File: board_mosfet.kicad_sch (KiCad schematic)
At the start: 7 parts

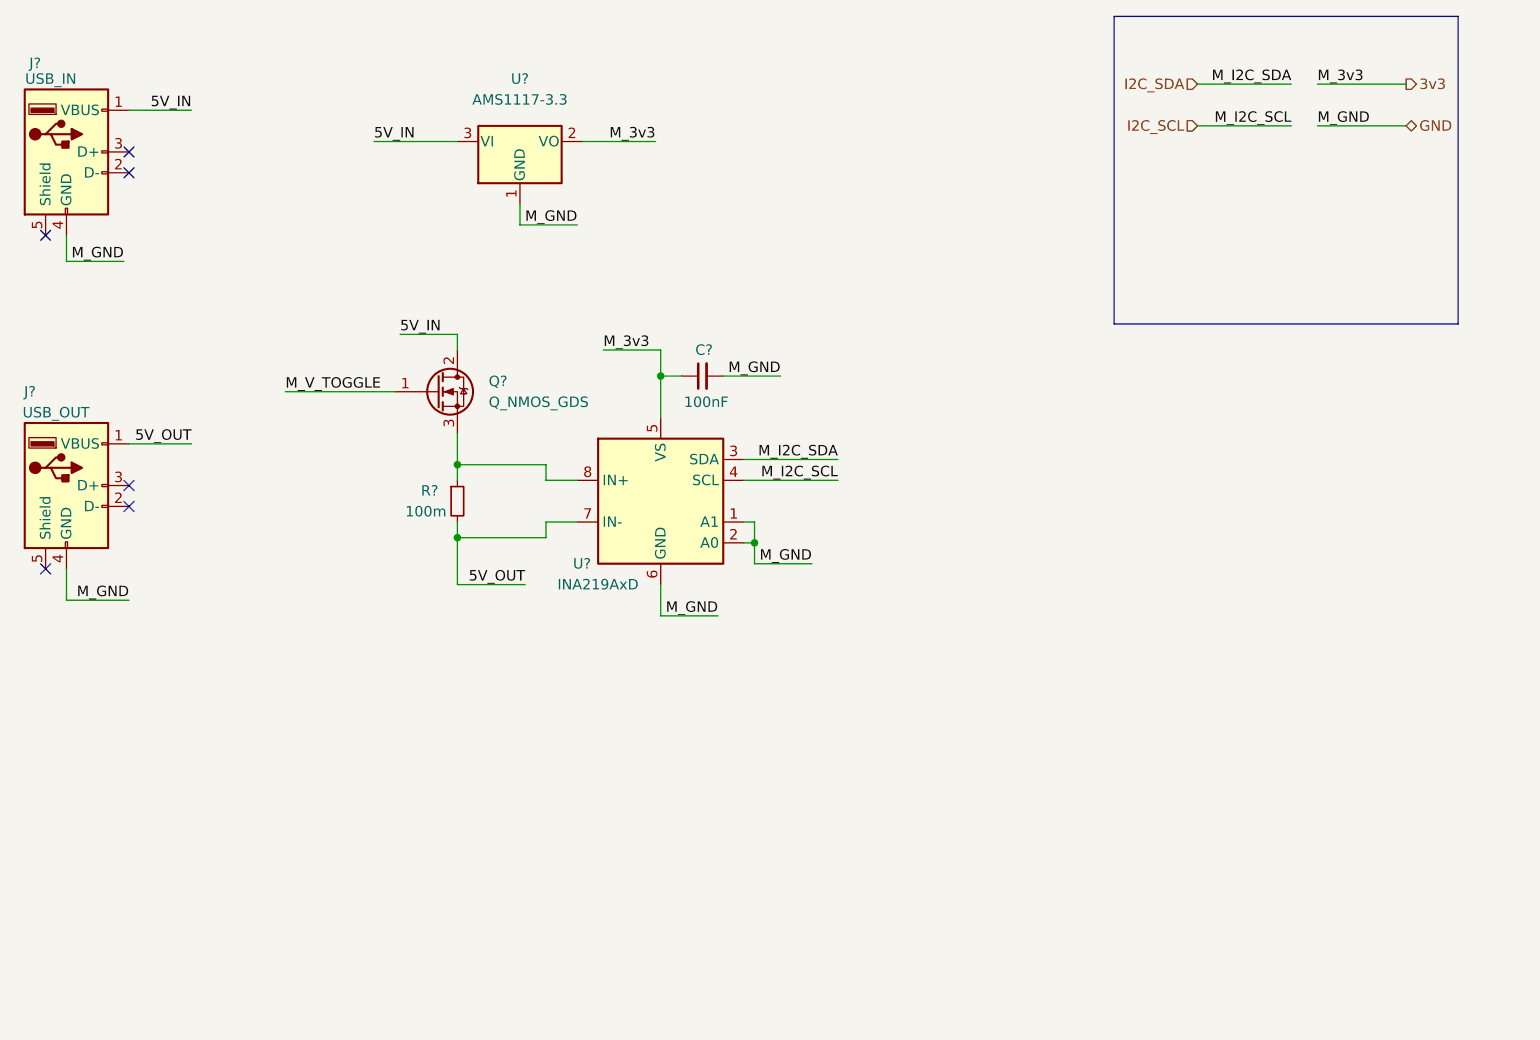
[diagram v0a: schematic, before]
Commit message: Fixed file name, started board layout
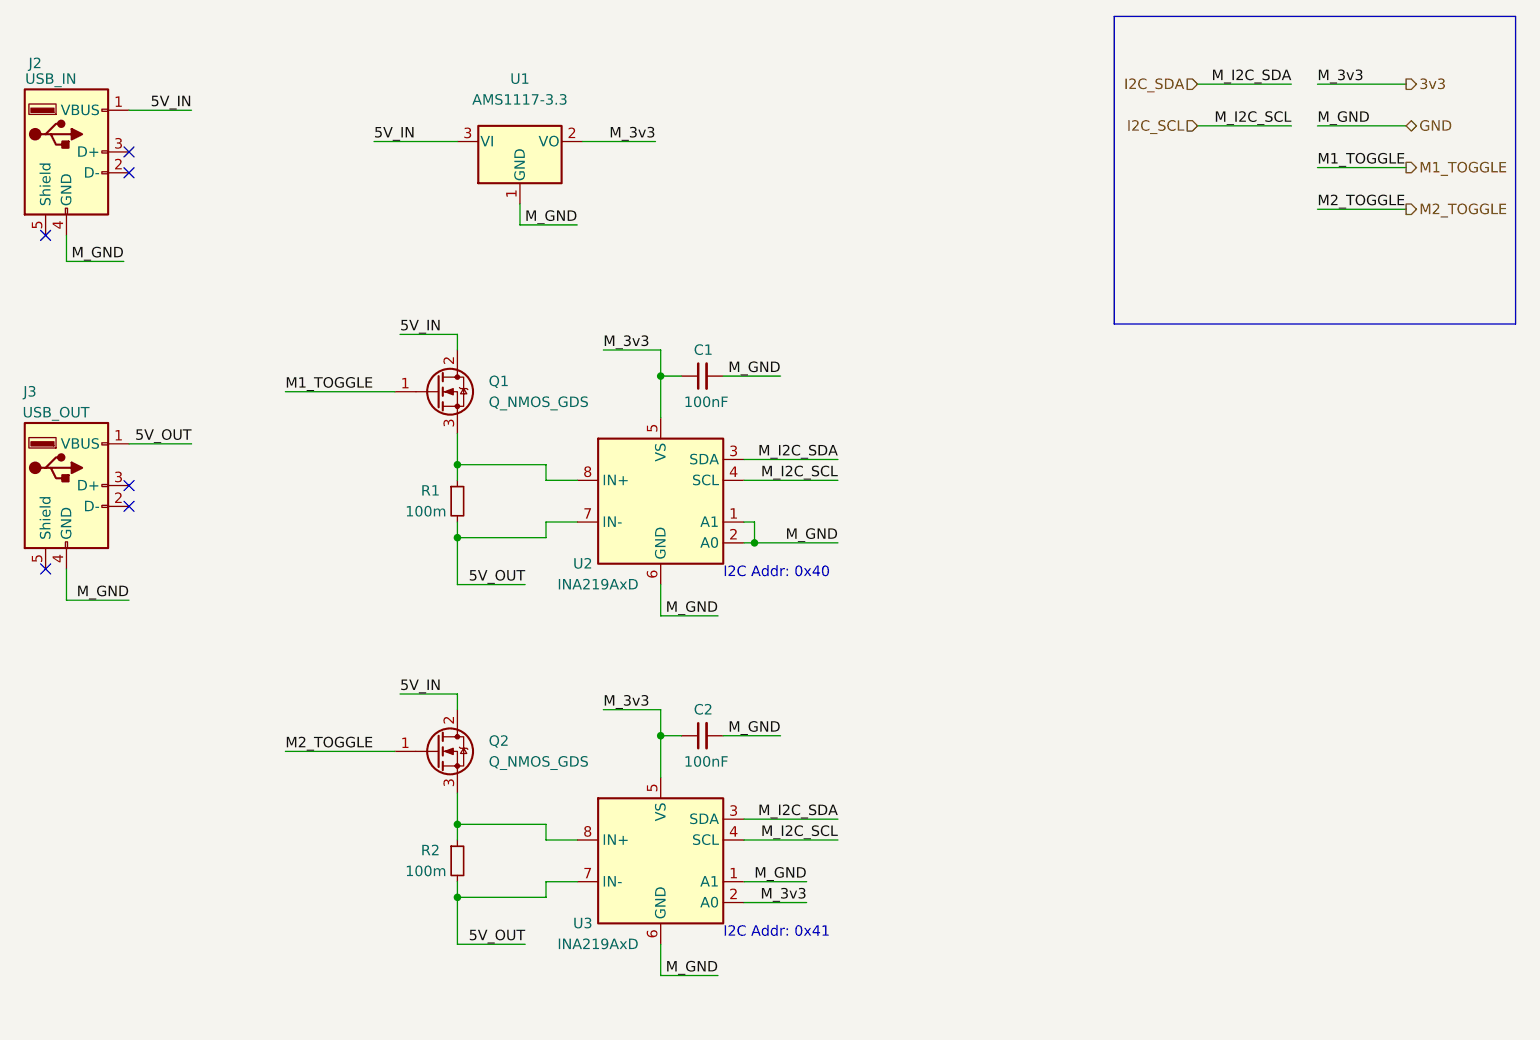
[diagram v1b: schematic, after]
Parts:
- added C2: 100nF, Capacitor_SMD:C_0402_1005Metric, symbol Device:C_Small
- added Q2: Q_NMOS_GDS, symbol Device:Q_NMOS_GDS
- added R2: 100m, Resistor_SMD:R_0402_1005Metric, symbol Device:R_Small
- added U3: INA219AxD, Package_SO:SOIC-8_3.9x4.9mm_P1.27mm, symbol Analog_ADC:INA219AxD
- C1: renamed from C?; footprint (none) -> Capacitor_SMD:C_0402_1005Metric
- R1: renamed from R?; footprint (none) -> Resistor_SMD:R_0402_1005Metric
- gave numbers to parts that had none: 5
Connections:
- net 3v3: now also C2.1, U3.2 (A0), U3.5 (VS)
- net 5V_IN: now also Q2.2 (D)
- net 5V_OUT: now also R2.2, U3.7 (IN-)
- net GND: now also C2.2, U3.1 (A1), U3.6 (GND)
- net I2C_SCL: now also U3.4 (SCL)
- net I2C_SDA: now also U3.3 (SDA)
- net M_V_TOGGLE renamed M1_TOGGLE
- new net: Q2.3 (S), R2.1, U3.8 (IN+)
- new net M2_TOGGLE: Q2.1 (G)
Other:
- note added: "I2C Addr: 0x40"
- note added: "I2C Addr: 0x41"

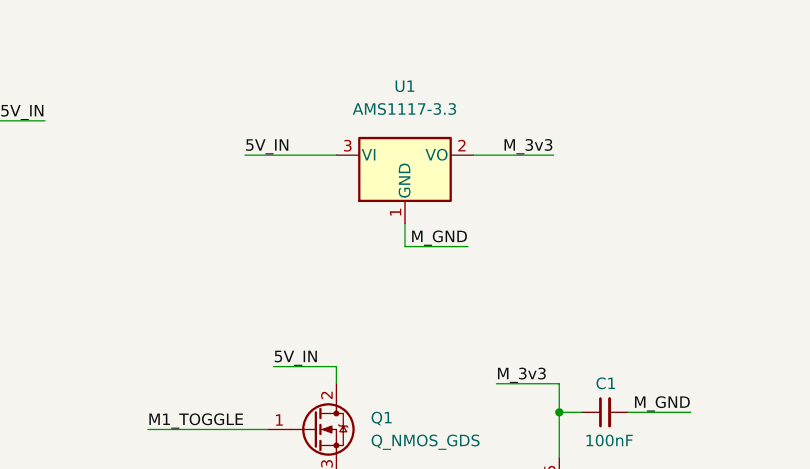
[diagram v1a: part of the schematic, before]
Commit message: Added capacitor filtering to AMS1117
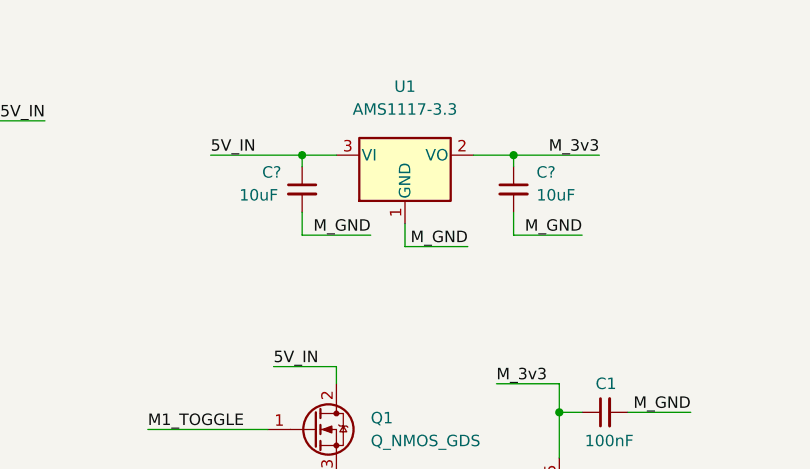
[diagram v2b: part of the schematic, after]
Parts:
- added C? (x2): 10uF, symbol Device:C_Small
- U1: LCSC Part Number (none) -> C173386; Manufacturer (none) -> Shenzhen Fuman Elec; Manufacturer Part Number (none) -> AMS1117-3.3V
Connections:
- net 3v3: now also C?.1
- net 5V_IN: now also C?.1
- net GND: now also C?.2, C?.2
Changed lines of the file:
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@@
   (junction (at 85.09 92.075) (diameter 0) (color 0 0 0 0)
   )
+  (junction (at 81.28 43.815) (diameter 0) (color 0 0 0 0)
+  )
   (junction (at 85.09 135.89) (diameter 0) (color 0 0 0 0)
+  )
+  (junction (at 104.775 43.815) (diameter 0) (color 0 0 0 0)
   )
   (no_connect (at 45.085 45.085))
@@
     (stroke (width 0) (type default) (color 0 0 0 0))
   )
+  (wire (pts (xy 104.775 43.815) (xy 114.3 43.815))
+    (stroke (width 0) (type default) (color 0 0 0 0))
+  )
   (wire (pts (xy 175.26 36.83) (xy 186.69 36.83))
     (stroke (width 0) (type default) (color 0 0 0 0))
@@
     (stroke (width 0) (type default) (color 0 0 0 0))
   )
+  (wire (pts (xy 104.775 52.705) (xy 104.775 50.165))
+    (stroke (width 0) (type default) (color 0 0 0 0))
+  )
   (wire (pts (xy 120.015 85.09) (xy 131.445 85.09))
     (stroke (width 0) (type default) (color 0 0 0 0))
@@
     (stroke (width 0) (type default) (color 0 0 0 0))
   )
-  (wire (pts (xy 74.93 43.815) (xy 85.09 43.815))
+  (wire (pts (xy 71.12 43.815) (xy 81.28 43.815))
     (stroke (width 0) (type default) (color 0 0 0 0))
   )
@@
     (stroke (width 0) (type default) (color 0 0 0 0))
   )
+  (wire (pts (xy 81.28 52.705) (xy 81.28 50.165))
+    (stroke (width 0) (type default) (color 0 0 0 0))
+  )
   (wire (pts (xy 93.345 97.79) (xy 85.09 97.79))
     (stroke (width 0) (type default) (color 0 0 0 0))
@@
     (stroke (width 0) (type default) (color 0 0 0 0))
   )
+  (wire (pts (xy 81.28 43.815) (xy 81.28 45.085))
+    (stroke (width 0) (type default) (color 0 0 0 0))
+  )
   (wire (pts (xy 189.865 36.83) (xy 200.66 36.83))
     (stroke (width 0) (type default) (color 0 0 0 0))
   )
-  (wire (pts (xy 100.33 43.815) (xy 109.22 43.815))
+  (wire (pts (xy 100.33 43.815) (xy 104.775 43.815))
     (stroke (width 0) (type default) (color 0 0 0 0))
   )
@@
     (stroke (width 0) (type default) (color 0 0 0 0))
   )
+  (wire (pts (xy 88.9 52.705) (xy 81.28 52.705))
+    (stroke (width 0) (type default) (color 0 0 0 0))
+  )
   (wire (pts (xy 102.87 113.03) (xy 109.855 113.03))
     (stroke (width 0) (type default) (color 0 0 0 0))
   )
+  (wire (pts (xy 104.775 43.815) (xy 104.775 45.085))
+    (stroke (width 0) (type default) (color 0 0 0 0))
+  )
   (wire (pts (xy 37.465 55.245) (xy 37.465 58.42))
     (stroke (width 0) (type default) (color 0 0 0 0))
@@
     (stroke (width 0) (type default) (color 0 0 0 0))
   )
+  (wire (pts (xy 112.395 52.705) (xy 104.775 52.705))
+    (stroke (width 0) (type default) (color 0 0 0 0))
+  )
   (wire (pts (xy 109.855 97.79) (xy 109.855 101.6))
     (stroke (width 0) (type default) (color 0 0 0 0))
@@
     (stroke (width 0) (type default) (color 0 0 0 0))
   )
+  (wire (pts (xy 81.28 43.815) (xy 85.09 43.815))
+    (stroke (width 0) (type default) (color 0 0 0 0))
+  )
   (text "I2C Addr: 0x41" (at 117.475 140.97 0)
     (effects (font (size 1.27 1.27)) (justify left bottom))
@@
     (effects (font (size 1.27 1.27)) (justify left bottom))
   )
+  (label "M_GND" (at 112.395 52.705 180)
+    (effects (font (size 1.27 1.27)) (justify right bottom))
+  )
   (label "5V_OUT" (at 52.705 80.645 180)
     (effects (font (size 1.27 1.27)) (justify right bottom))
@@
     (effects (font (size 1.27 1.27)) (justify right bottom))
   )
-  (label "M_3v3" (at 109.22 43.815 180)
+  (label "M_3v3" (at 114.3 43.815 180)
     (effects (font (size 1.27 1.27)) (justify right bottom))
   )
@@
     (effects (font (size 1.27 1.27)) (justify right bottom))
   )
+  (label "M_GND" (at 88.9 52.705 180)
+    (effects (font (size 1.27 1.27)) (justify right bottom))
+  )
   (label "5V_OUT" (at 93.345 97.79 180)
     (effects (font (size 1.27 1.27)) (justify right bottom))
   )
-  (label "5V_IN" (at 74.93 43.815 0)
+  (label "5V_IN" (at 71.12 43.815 0)
     (effects (font (size 1.27 1.27)) (justify left bottom))
   )
@@
     (pin "2")
   )
+  (symbol (lib_id "Device:C_Small") (at 81.28 47.625 0) (unit 1)
+    (in_bom yes) (on_board yes)
+    (property "Reference" "C?" (id 0) (at 76.835 45.7262 0)
+      (effects (font (size 1.27 1.27)) (justify left))
+    )
+    (property "Value" "10uF" (id 1) (at 74.295 48.2662 0)
+      (effects (font (size 1.27 1.27)) (justify left))
+    )
+    (property "Footprint" "" (id 2) (at 81.28 47.625 0)
+      (effects (font (size 1.27 1.27)) hide)
+    )
+    (property "Datasheet" "~" (id 3) (at 81.28 47.625 0)
+      (effects (font (size 1.27 1.27)) hide)
+    )
+    (pin "1")
+    (pin "2")
+  )
   (symbol (lib_id "Device:R_Small") (at 85.09 87.63 0) (unit 1)
     (in_bom yes) (on_board yes)
@@
     )
     (property "Datasheet" "~" (id 3) (at 114.935 72.39 0)
+      (effects (font (size 1.27 1.27)) hide)
+    )
+    (pin "1")
+    (pin "2")
+  )
+  (symbol (lib_id "Device:C_Small") (at 104.775 47.625 0) (unit 1)
+    (in_bom yes) (on_board yes)
+    (property "Reference" "C?" (id 0) (at 107.315 45.7262 0)
+      (effects (font (size 1.27 1.27)) (justify left))
+    )
+    (property "Value" "10uF" (id 1) (at 107.315 48.2662 0)
+      (effects (font (size 1.27 1.27)) (justify left))
+    )
+    (property "Footprint" "" (id 2) (at 104.775 47.625 0)
+      (effects (font (size 1.27 1.27)) hide)
+    )
+    (property "Datasheet" "~" (id 3) (at 104.775 47.625 0)
       (effects (font (size 1.27 1.27)) hide)
     )
@@
       (effects (font (size 1.27 1.27)) hide)
     )
+    (property "LCSC Part Number" "C173386" (id 4) (at 92.71 43.815 0)
+      (effects (font (size 1.27 1.27)) hide)
+    )
+    (property "Manufacturer" "Shenzhen Fuman Elec" (id 5) (at 92.71 43.815 0)
+      (effects (font (size 1.27 1.27)) hide)
+    )
+    (property "Manufacturer Part Number" "AMS1117-3.3V" (id 6) (at 92.71 43.815 0)
+      (effects (font (size 1.27 1.27)) hide)
+    )
